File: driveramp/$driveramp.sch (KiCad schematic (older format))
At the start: 53 parts, among them J1 SMA, J2 SMA, P1 FAULT, P2 CONN_2, T1 MABA-011002, T2 2x Fair-Rite 2843006802, coax, U1 LM2936HVBMA-5.0, U2 MRFE6VP100H

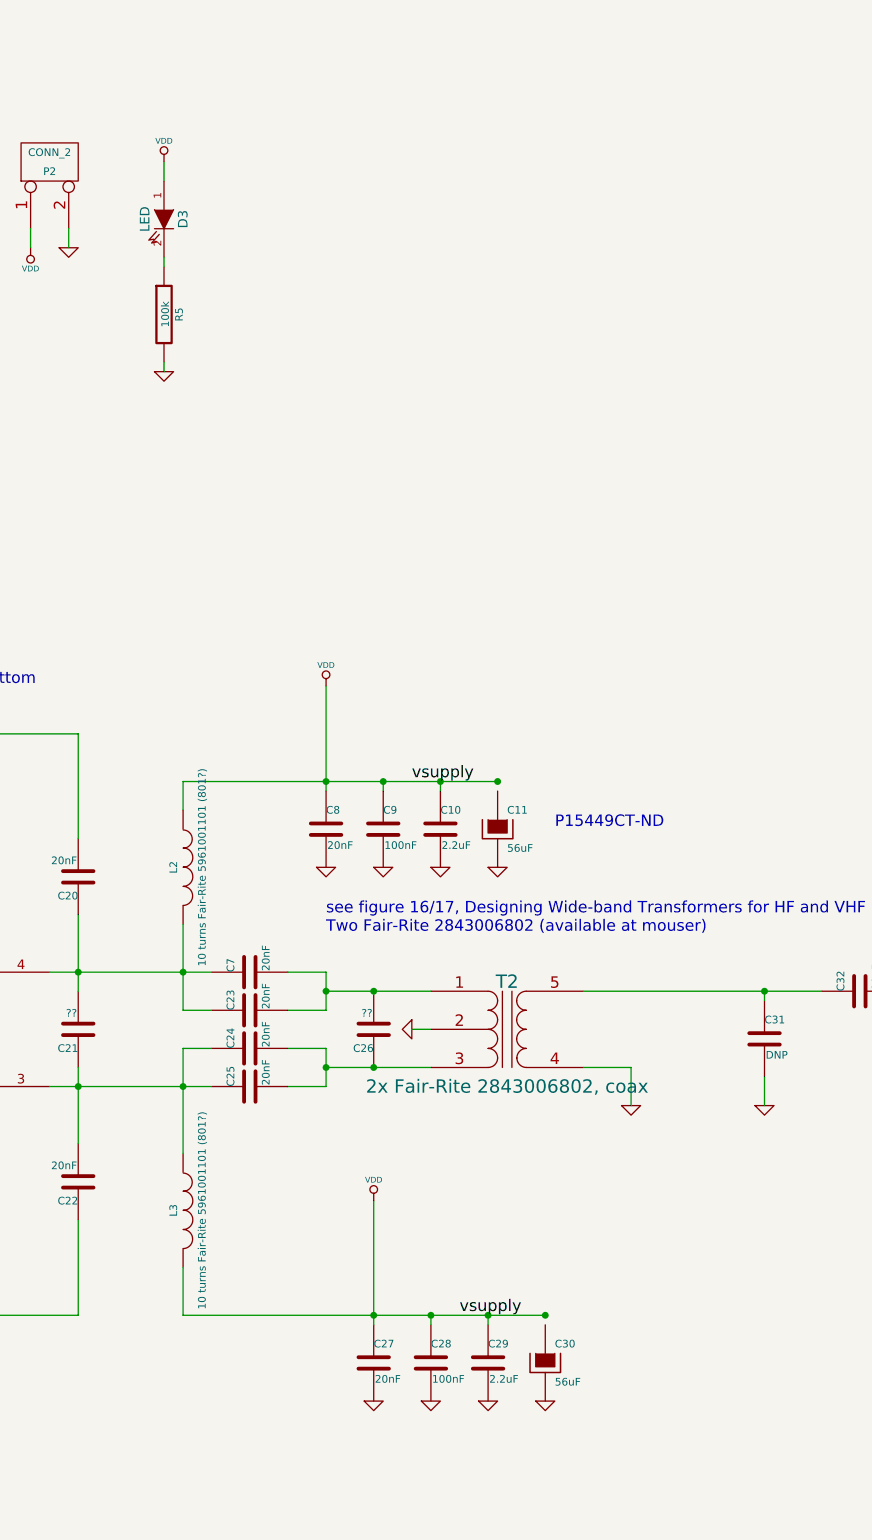
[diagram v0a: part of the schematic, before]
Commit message: changed driver amp to push-pull
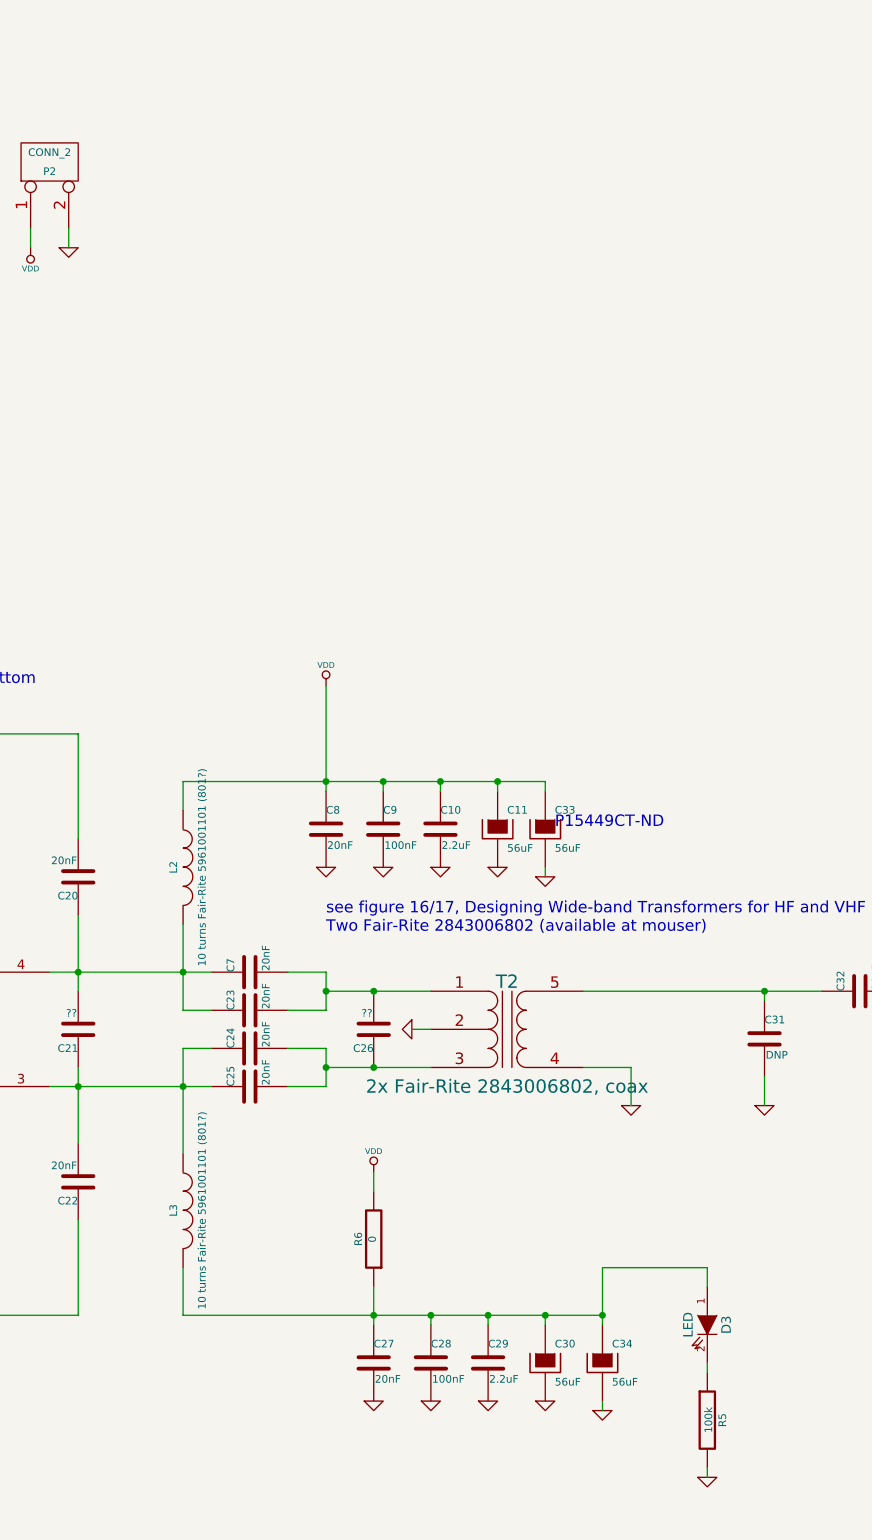
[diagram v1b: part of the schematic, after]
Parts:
- added C33, C34: 56uF, Capacitors_SMD:c_elec_10x10, symbol CAPAPOL
- added R6: 0, symbol R
- C1: footprint Capacitors_SMD:c_2225 -> Capacitors_SMD:c_1210
- D2: footprint (none) -> Diodes_SMD:Diode-SMB_Handsoldering
- D3: footprint (none) -> LEDs:LED-0603
- L1: footprint (none) -> Choke_Toroid_ThroughHole:Choke_Toroid_8x16mm_Vertical
- R1, R4: footprint Resistors_ThroughHole:Resistor_Horizontal_RM15mm -> local:4122
- R5: footprint (none) -> SMD_Packages:SM0805
- T1: footprint (none) -> local:MABA-01002
- T2: footprint (none) -> local:2843006802
- U2: footprint (none) -> local:NI780-4
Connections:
- net GND: now also C33.2, C34.2
- net VDD: now also C11.1, C33.1, R6.2; no longer C27.1, C28.1, C29.1, D3.1 (A), L3.2
- net at C30.1: now also C27.1, C28.1, C29.1, D3.1 (A), L3.2, C34.1, R6.1
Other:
- moved on the sheet: D3, R5
